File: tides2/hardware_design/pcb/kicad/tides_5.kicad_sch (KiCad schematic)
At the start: 42 parts

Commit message: replace tssop tlv op amp with soic
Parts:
- IC8, IC9: footprint (none) -> Package_SO:SOIC-14_3.9x8.7mm_P1.27mm
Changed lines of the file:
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@@
       (effects (font (size 1.778 1.5113)) (justify left bottom) hide)
     )
-    (property "Footprint" "" (id 2) (at 345.44 195.58 0)
+    (property "Footprint" "Package_SO:SOIC-14_3.9x8.7mm_P1.27mm" (id 2) (at 345.44 195.58 0)
       (effects (font (size 1.27 1.27)) hide)
     )
@@
       (effects (font (size 1.778 1.5113)) (justify left bottom) hide)
     )
-    (property "Footprint" "" (id 2) (at 172.72 144.78 0)
+    (property "Footprint" "Package_SO:SOIC-14_3.9x8.7mm_P1.27mm" (id 2) (at 172.72 144.78 0)
       (effects (font (size 1.27 1.27)) hide)
     )
@@
       (effects (font (size 1.778 1.5113)) (justify left bottom) hide)
     )
-    (property "Footprint" "" (id 2) (at 182.88 114.3 0)
+    (property "Footprint" "Package_SO:SOIC-14_3.9x8.7mm_P1.27mm" (id 2) (at 182.88 114.3 0)
       (effects (font (size 1.27 1.27)) hide)
     )
@@
       (effects (font (size 1.778 1.5113)) (justify left bottom) hide)
     )
-    (property "Footprint" "" (id 2) (at 269.24 218.44 0)
+    (property "Footprint" "Package_SO:SOIC-14_3.9x8.7mm_P1.27mm" (id 2) (at 269.24 218.44 0)
       (effects (font (size 1.27 1.27)) hide)
     )
@@
       (effects (font (size 1.778 1.5113)) (justify left bottom) hide)
     )
-    (property "Footprint" "" (id 2) (at 279.4 187.96 0)
+    (property "Footprint" "Package_SO:SOIC-14_3.9x8.7mm_P1.27mm" (id 2) (at 279.4 187.96 0)
       (effects (font (size 1.27 1.27)) hide)
     )
@@
       (effects (font (size 1.778 1.5113)) (justify left bottom) hide)
     )
-    (property "Footprint" "" (id 2) (at 276.86 111.76 0)
+    (property "Footprint" "Package_SO:SOIC-14_3.9x8.7mm_P1.27mm" (id 2) (at 276.86 111.76 0)
       (effects (font (size 1.27 1.27)) hide)
     )
@@
       (effects (font (size 1.778 1.5113)) (justify left bottom) hide)
     )
-    (property "Footprint" "" (id 2) (at 266.7 142.24 0)
+    (property "Footprint" "Package_SO:SOIC-14_3.9x8.7mm_P1.27mm" (id 2) (at 266.7 142.24 0)
       (effects (font (size 1.27 1.27)) hide)
     )
@@
       (effects (font (size 1.778 1.5113)) (justify left bottom) hide)
     )
-    (property "Footprint" "" (id 2) (at 350.52 195.58 0)
+    (property "Footprint" "Package_SO:SOIC-14_3.9x8.7mm_P1.27mm" (id 2) (at 350.52 195.58 0)
       (effects (font (size 1.27 1.27)) hide)
     )
@@
       (effects (font (size 1.778 1.5113)) (justify left bottom) hide)
     )
-    (property "Footprint" "" (id 2) (at 172.72 218.44 0)
+    (property "Footprint" "Package_SO:SOIC-14_3.9x8.7mm_P1.27mm" (id 2) (at 172.72 218.44 0)
       (effects (font (size 1.27 1.27)) hide)
     )
@@
       (effects (font (size 1.778 1.5113)) (justify left bottom) hide)
     )
-    (property "Footprint" "" (id 2) (at 182.88 187.96 0)
-      (effects (font (size 1.27 1.27)) hide)
-    )
+    (property "Footprint" "Package_SO:SOIC-14_3.9x8.7mm_P1.27mm" (id 2) (at 182.88 187.96 0)
+      (effects (font (size 1.27 1.27)) hide)
+    )

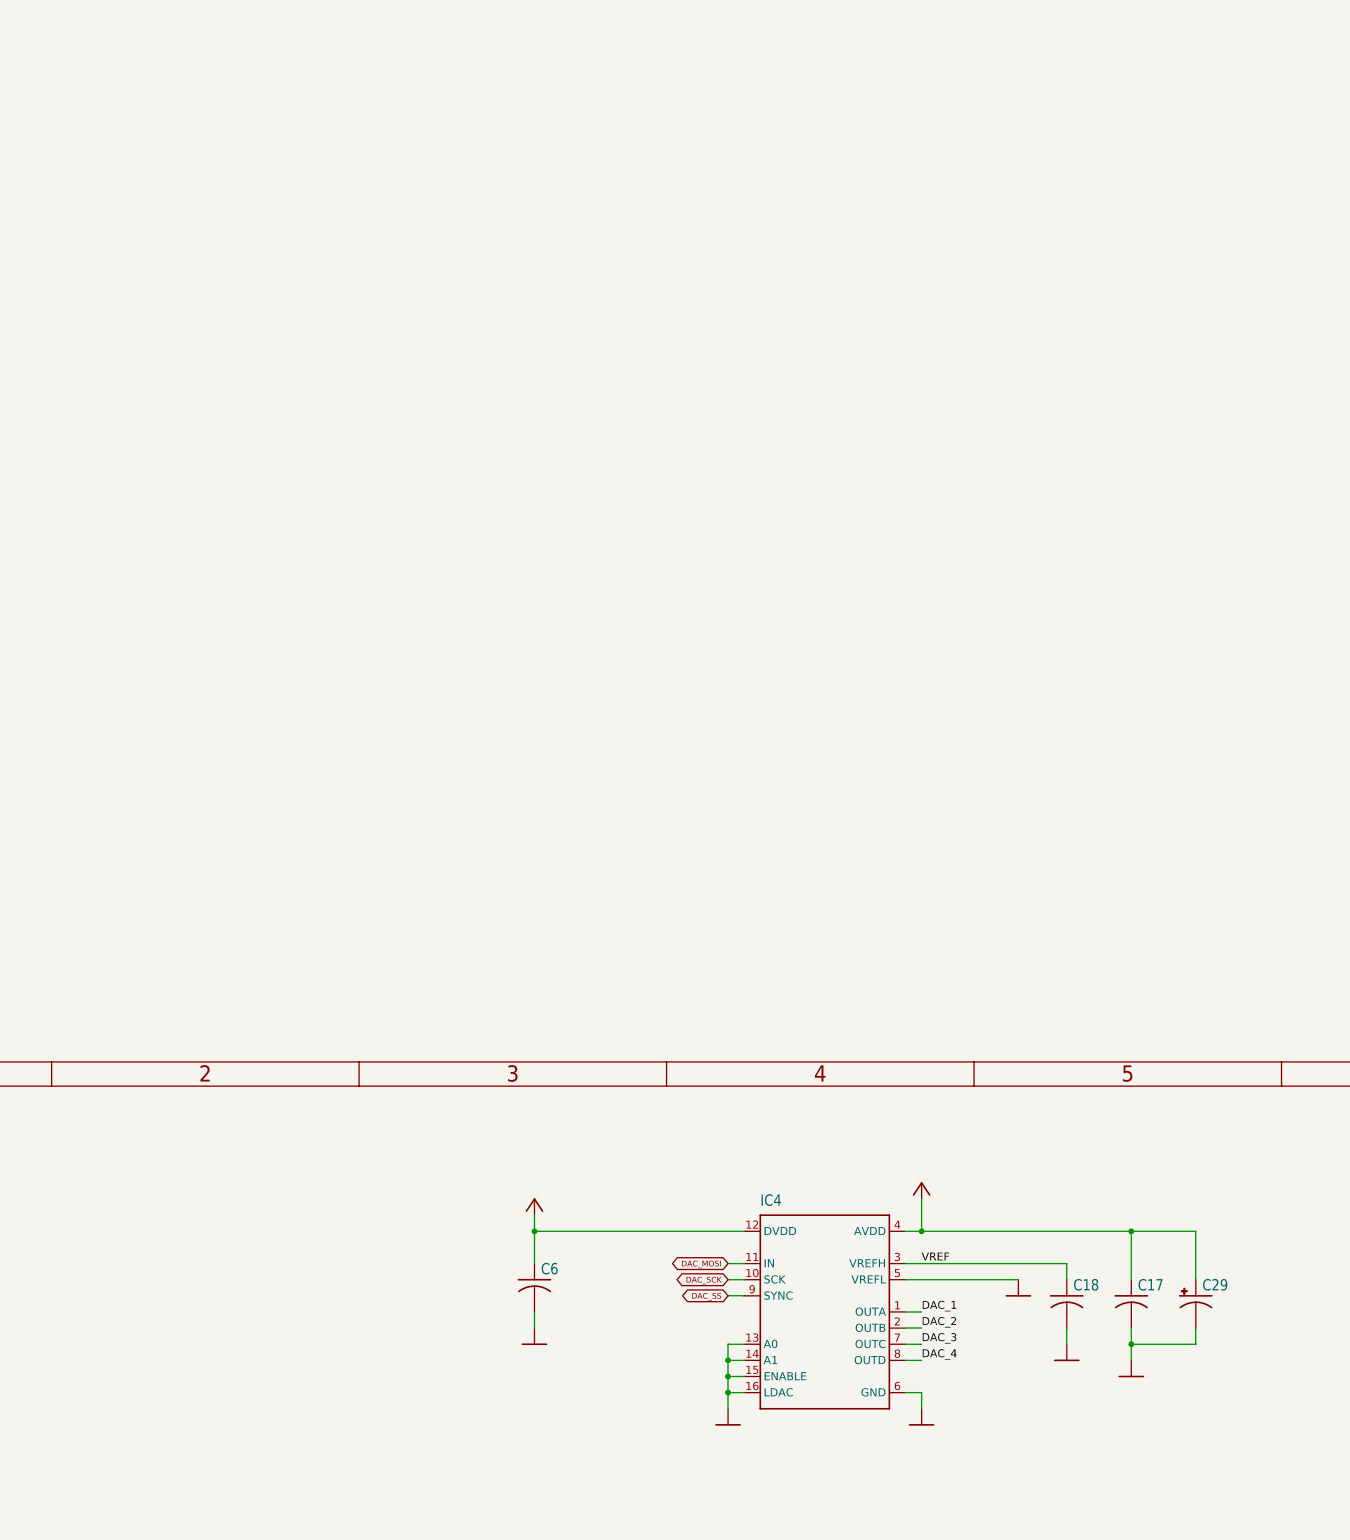
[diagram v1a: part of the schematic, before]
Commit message: tides2 dac8164 -> dac8565
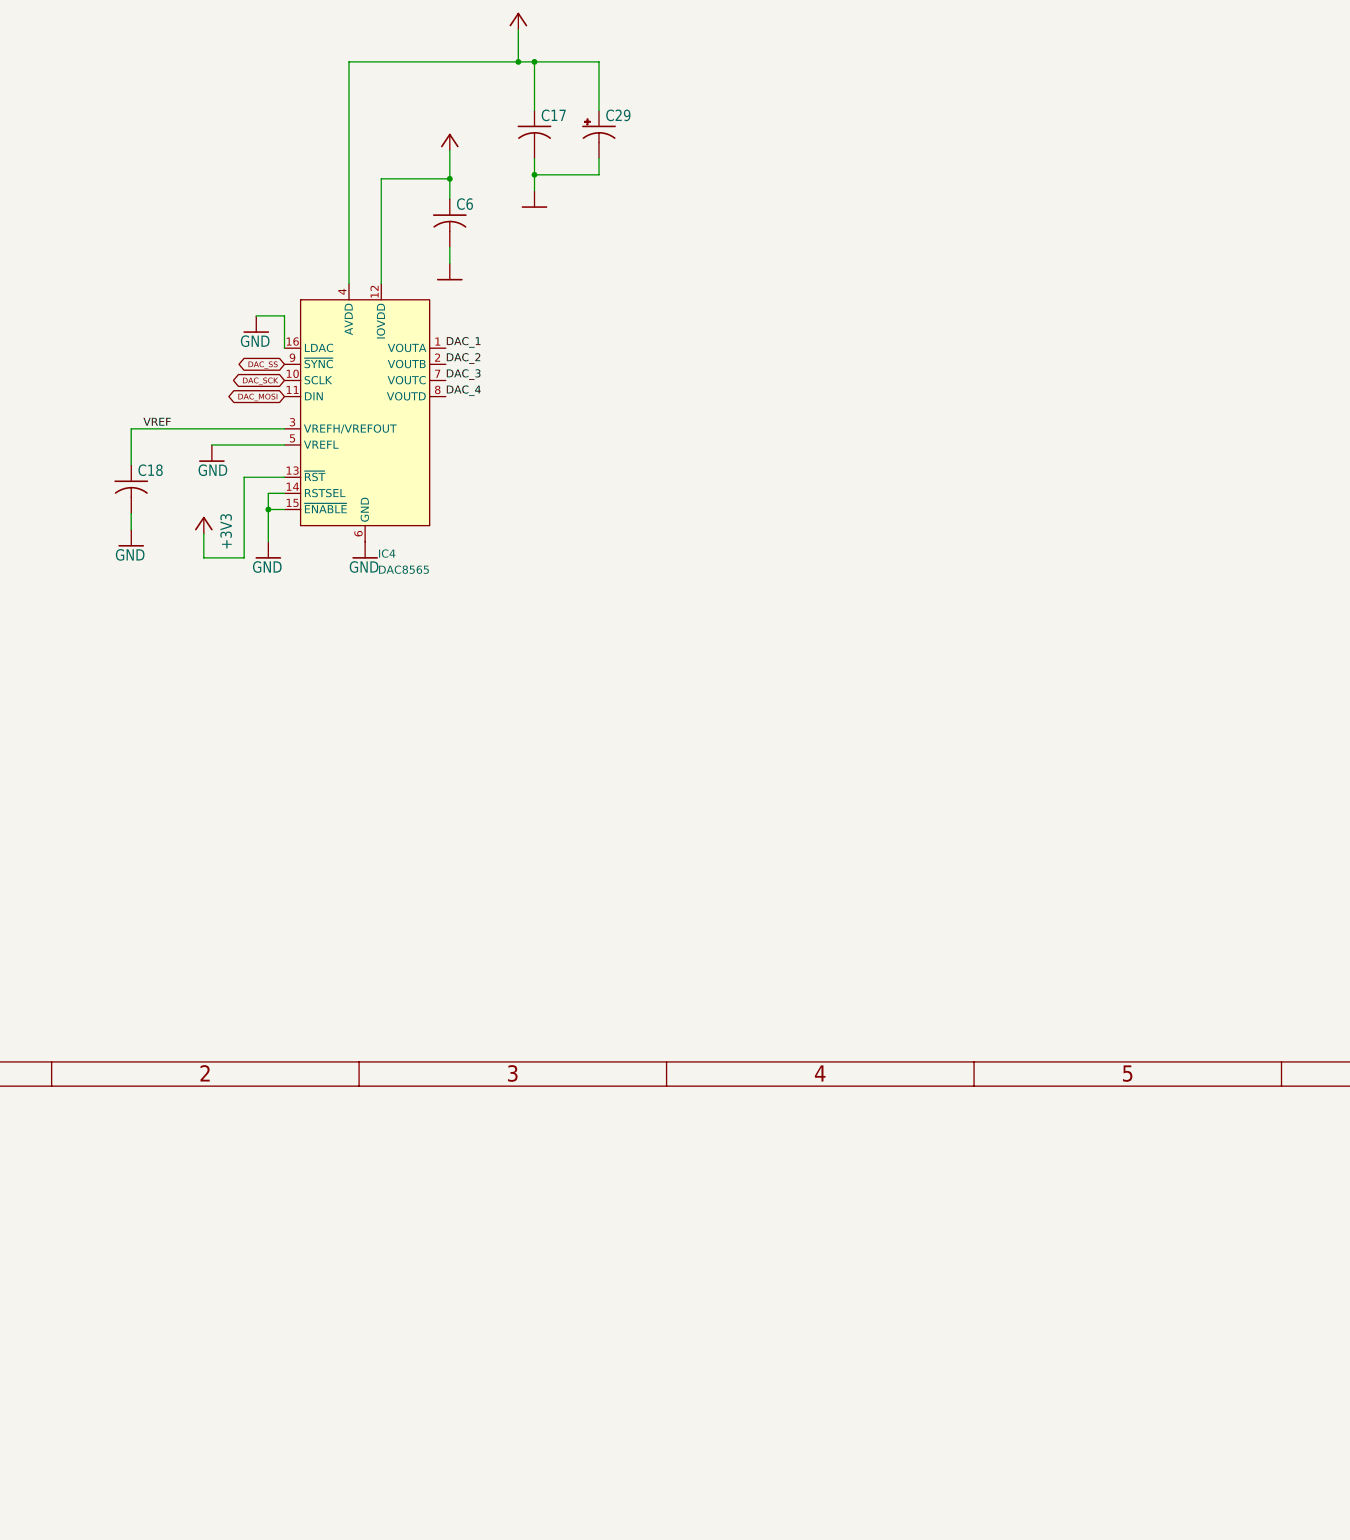
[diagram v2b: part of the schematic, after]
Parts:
- removed IC4: (no value), symbol tides-eagle-import:DAC8564
- added IC4: DAC8565, Package_SO:TSSOP-16_4.4x5mm_P0.65mm, symbol Analog_DAC:DAC8565
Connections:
- net +3V3: now also IC4.12 (IOVDD), IC4.13 (~{RST})
- net +3V3_A: now also IC4.4 (AVDD)
- net DAC_1: now also IC4.1 (VOUTA)
- net DAC_2: now also IC4.2 (VOUTB)
- net DAC_3: now also IC4.7 (VOUTC)
- net DAC_4: now also IC4.8 (VOUTD)
- net DAC_MOSI: now also IC4.11 (DIN)
- net DAC_SCK: now also IC4.10 (SCLK)
- net DAC_SS: now also IC4.9 (~{SYNC})
- net GND: now also IC4.14 (RSTSEL), IC4.15 (~{ENABLE}), IC4.16 (LDAC), IC4.5 (VREFL), IC4.6 (GND)
- net VREF: now also IC4.3 (VREFH/VREFOUT)
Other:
- moved on the sheet: C17, C18, C29, C6

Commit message: tides final tweaks
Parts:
- C17, C33, C34, C48, C49, C6: value (none) -> 100n; footprint (none) -> tides:C0402
- C18, C21: value (none) -> 1u; footprint (none) -> tides:C0402
- C29: value (none) -> 10u; footprint (none) -> tides:PANASONIC_B
- C37, C38, C39, C40: value (none) -> 47p; footprint (none) -> tides:C0402
- IC8, IC9: value (none) -> TLV4172
- J10, J11, J12, J9: value (none) -> PJ301_THONKICONN6; footprint (none) -> tides:WQP_PJ_301M6
- LED4, LED5, LED6, LED7: value (none) -> 3BC-F; footprint (none) -> tides:LED3MM
- R14, R38, R39, R40, R42: value (none) -> 130k; footprint (none) -> tides:R0402
- R15: value (none) -> 100k; footprint (none) -> tides:R0402
- R31, R32, R33, R34: value (none) -> 20k; footprint (none) -> tides:R0402
- R45, R47, R48, R49: value (none) -> 1.0k; footprint (none) -> tides:R0603
- R64, R65, R66, R67: value (none) -> 1.0k; footprint (none) -> tides:R0402
